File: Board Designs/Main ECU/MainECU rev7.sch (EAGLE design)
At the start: 203 parts, among them J1 JUMPER, J2 JUMPER, J3 JUMPER, J4 JUMPER, J5 JUMPER, J6 JUMPER, J7 JUMPER, J8 JUMPER, P1 SOLDER_PAD, P2 SOLDER_PAD, Q1 P-CHANNEL_MOSFET_DMP3099L-7, Q12 P-CHANNEL_MOSFET_DMP3099L-7, X1 CONNECTOR-37, X2 CONNECTOR-4AUTOSPORT, X3 CONNECTOR-4NANO-FIT-VERTICAL-4, X4 CONNECTOR-4NANO-FIT-VERTICAL-4

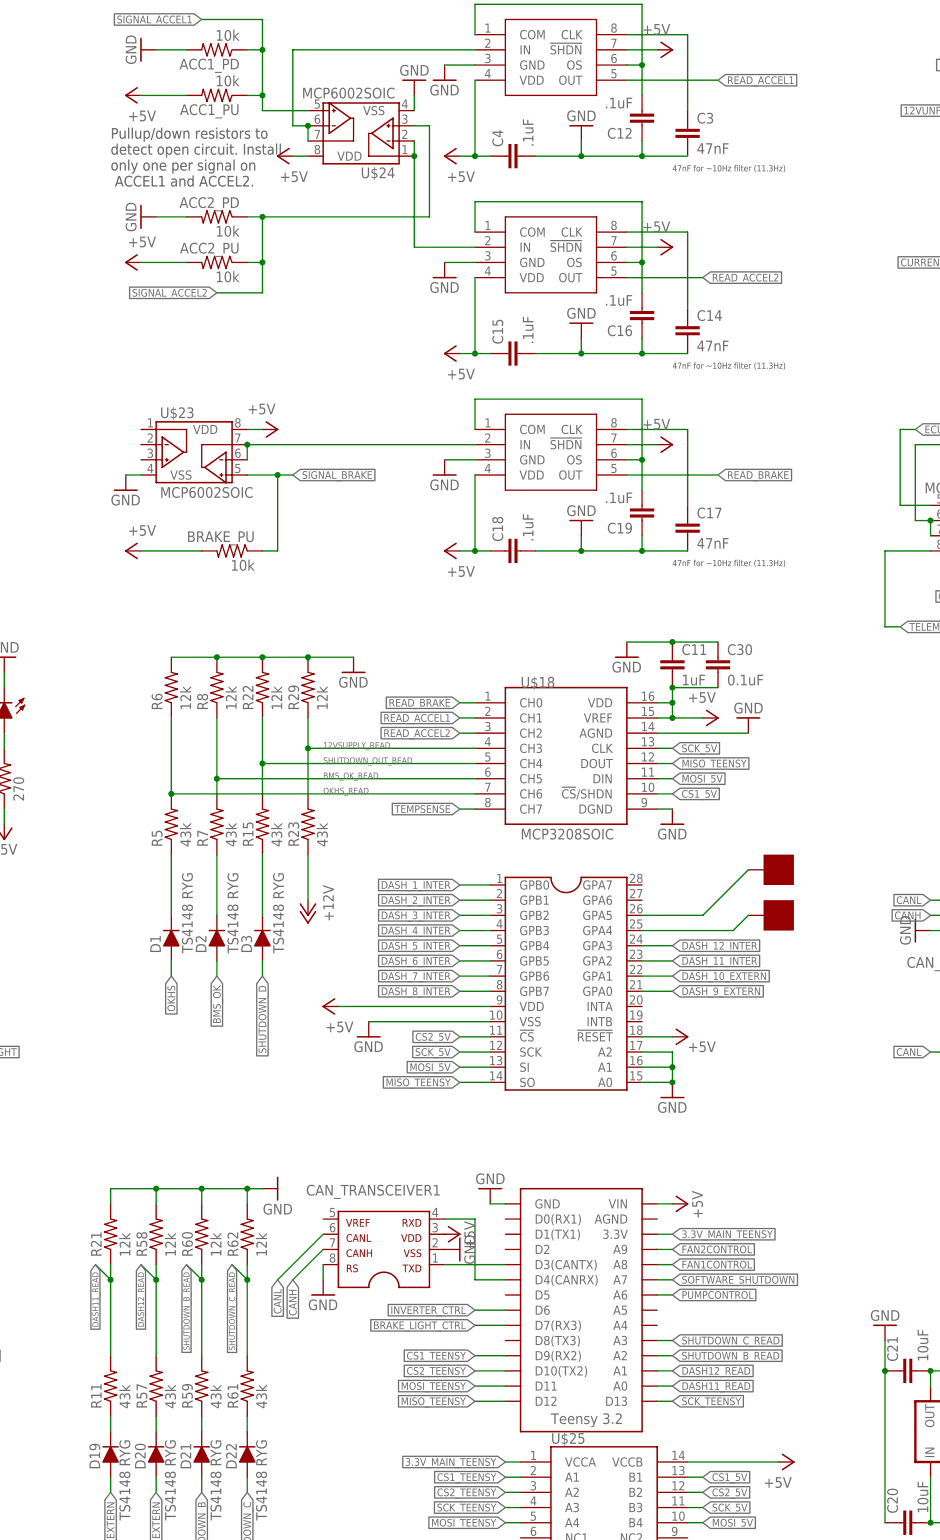
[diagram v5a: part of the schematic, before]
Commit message: Added bypass caps to transceiver, plus two op-amps, now need to do routing
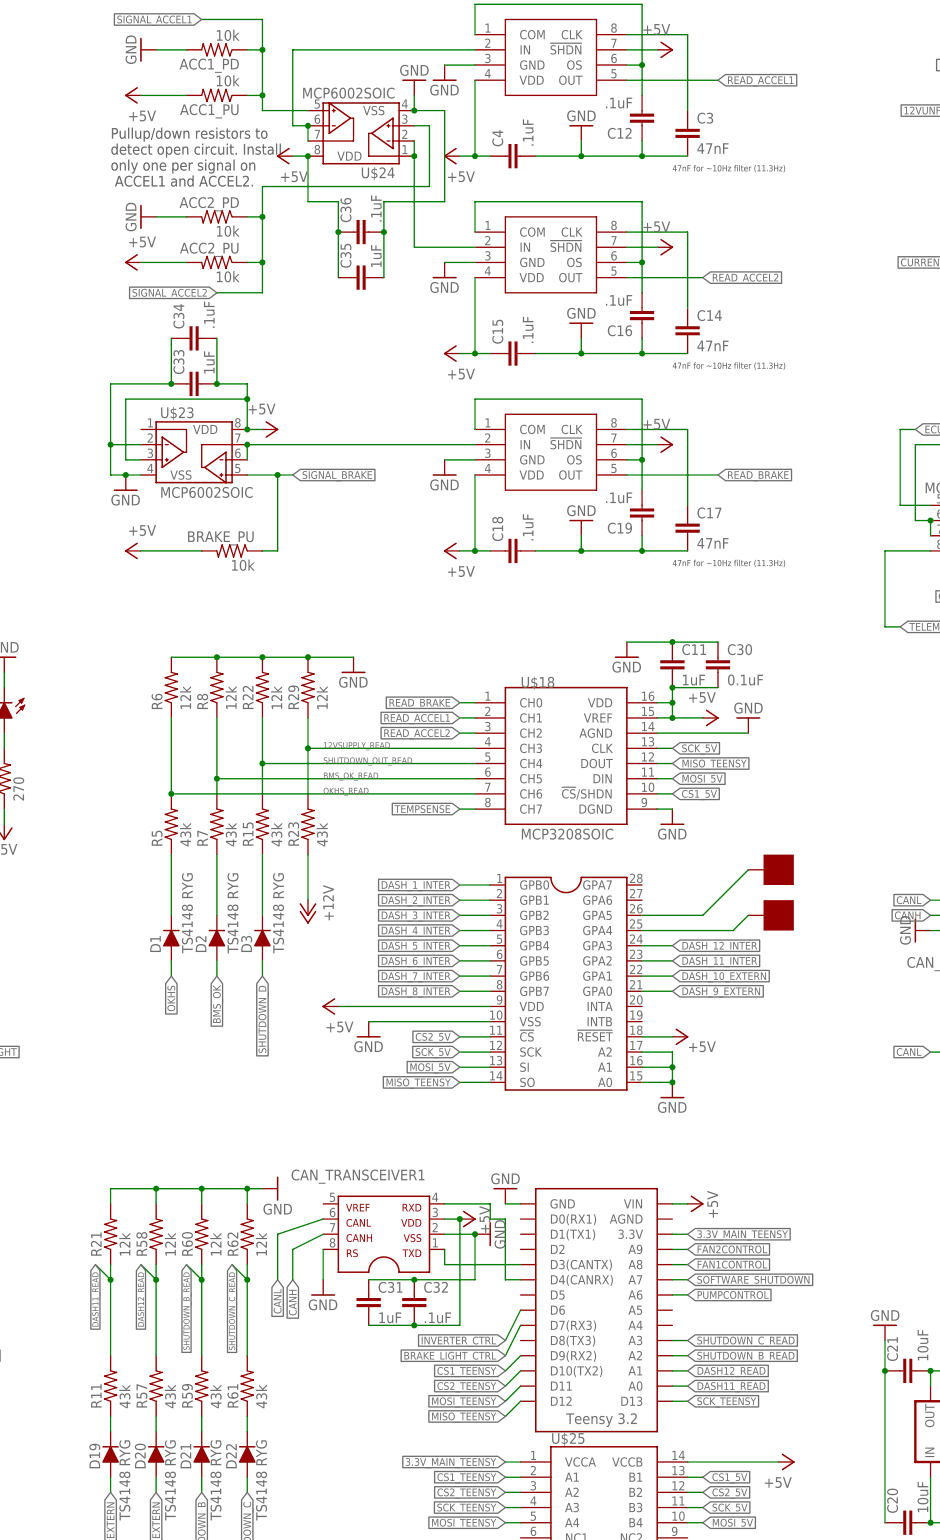
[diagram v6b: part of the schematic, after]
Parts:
- added C31, C33, C35: 1uF, HyTechDevices:CAP0805
- added C32, C34, C36: .1uF, HyTechDevices:CAP0805
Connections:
- net +5V: now also C31.2, C32.2, C33.2, C34.2, C35.1, C36.1, U$23.VINA+
- net GND: now also C31.1, C32.1, C33.1, C34.1, C35.2, C36.2, U$23.VINA-
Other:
- moved on the sheet: CAN_TRANSCEIVER1

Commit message: Main ECU: Add CAN tvs diode, Add filter to 12V sense, move components and traces; Library: Add CAN tvs diode
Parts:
- removed CAN_TRANSCEIVER2: MCP2551, HyTechDevices:MCP2551
- removed R46: 120, HyTechDevices:RESISTOR0805-RES
- added C37: 1uF, HyTechDevices:CAP0805
- added U$13: CDSOT23-T24CAN-Q, HyTechDevices:CDSOT23-T24CAN-Q
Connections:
- removed net N$62: CAN_TRANSCEIVER2.4, U$2.A15
- removed net N$64: CAN_TRANSCEIVER2.1, U$2.A14
- removed net TELEMETRY_CANH: CAN_TRANSCEIVER2.7, R46.2, X4-4.S
- removed net TELEMETRY_CANL: CAN_TRANSCEIVER2.6, R46.1, X4-3.S
- new net 12VSUPPLY_DIV: C37.2, R23.2, R29.1, U$23.VINA+
- net +5V: no longer U$23.VINA+
- net 12VSUPPLY_READ: now also U$23.VINA-, U$23.VOUTA; no longer R23.2, R29.1
- net CANH: now also U$13.2, X4-4.S
- net CANL: now also U$13.1, X4-3.S
- net GND: now also C37.1, U$13.3; no longer CAN_TRANSCEIVER2.2, CAN_TRANSCEIVER2.8, U$23.VINA-
- net TELEMETRY5V: no longer CAN_TRANSCEIVER2.3
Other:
- moved on the sheet: BRAKE_PU, C31, C32, C33, C34, C35, C36, R23, R29

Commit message: Main ECU: add capacitors
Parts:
- added C38, C39: 0.1uF, HyTechDevices:CAP0805
- added C40: 470uF, HyTechDevices:CAPPTH3
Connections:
- net +12V: now also C40.1
- net +5V: now also C38.1
- net GND: now also C38.2, C39.2, C40.2
- net VCC: now also C39.1
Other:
- moved on the sheet: LED11, R30, U$13
